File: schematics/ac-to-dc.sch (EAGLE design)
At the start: 12 parts, among them IC1 12V

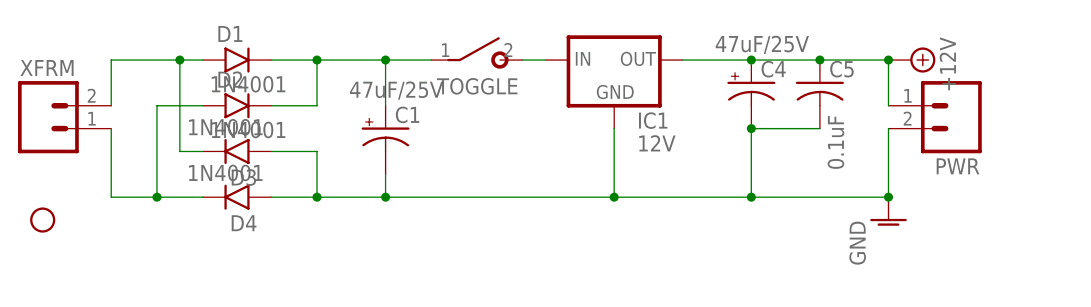
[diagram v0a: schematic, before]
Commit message: Added an LED to the ac-to-dc board
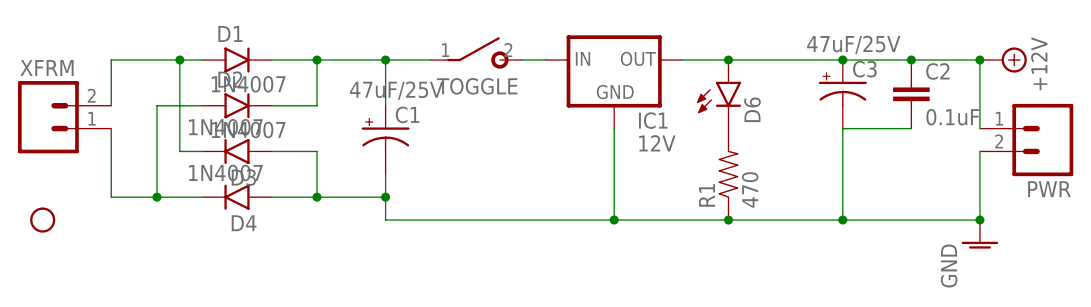
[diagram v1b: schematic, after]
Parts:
- removed C4: 47uF/25V, minimidi:CPOL-USE2.5-6
- removed C5: 0.1uF, minimidi:C-US025-025X050
- added C2: 0.1uF, SparkFun-Capacitors:CAPPTH
- added C3: 47uF/25V, minimidi:CPOL-USE2.5-6
- added D6: (no value), SparkFun-LED:LED-3MM-NO_SILK
- added R1: 470, SparkFun-Resistors:RESISTORPTH-1/4W
- D1, D2, D3, D4: value 1N4001 -> 1N4007
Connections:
- new net N$4: D6.C, R1.2
- net +12V: now also C2.1, C3.+, D6.A; no longer C4.+, C5.1
- net AGND: now also C2.2, C3.-, R1.1; no longer C4.-, C5.2
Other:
- moved on the sheet: PWR
